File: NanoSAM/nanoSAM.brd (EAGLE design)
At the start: 89.6 x 94 mm, 119 parts, among them J1 POWER_JACK, U1 LTC3260EMSEPBF, U2 LMV324

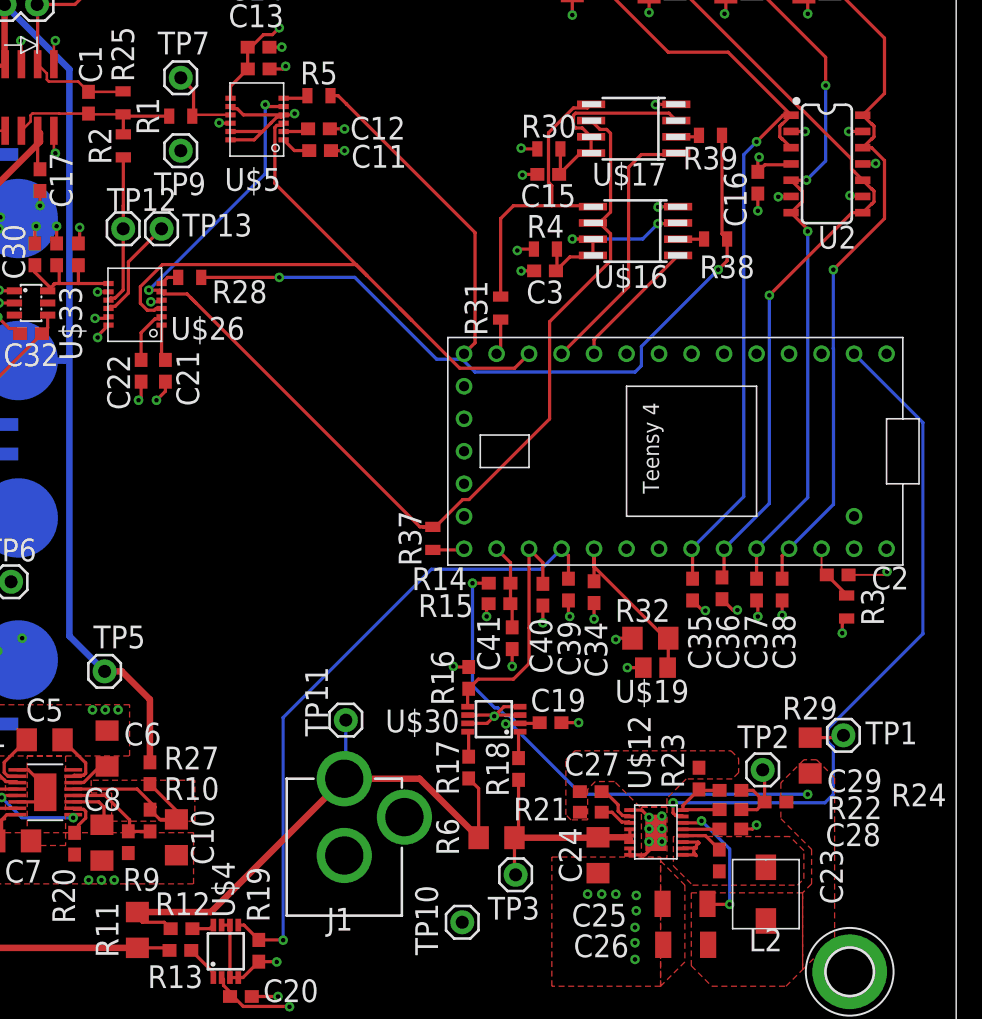
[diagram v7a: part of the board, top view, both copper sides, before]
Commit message: fixed footprint, broke other things
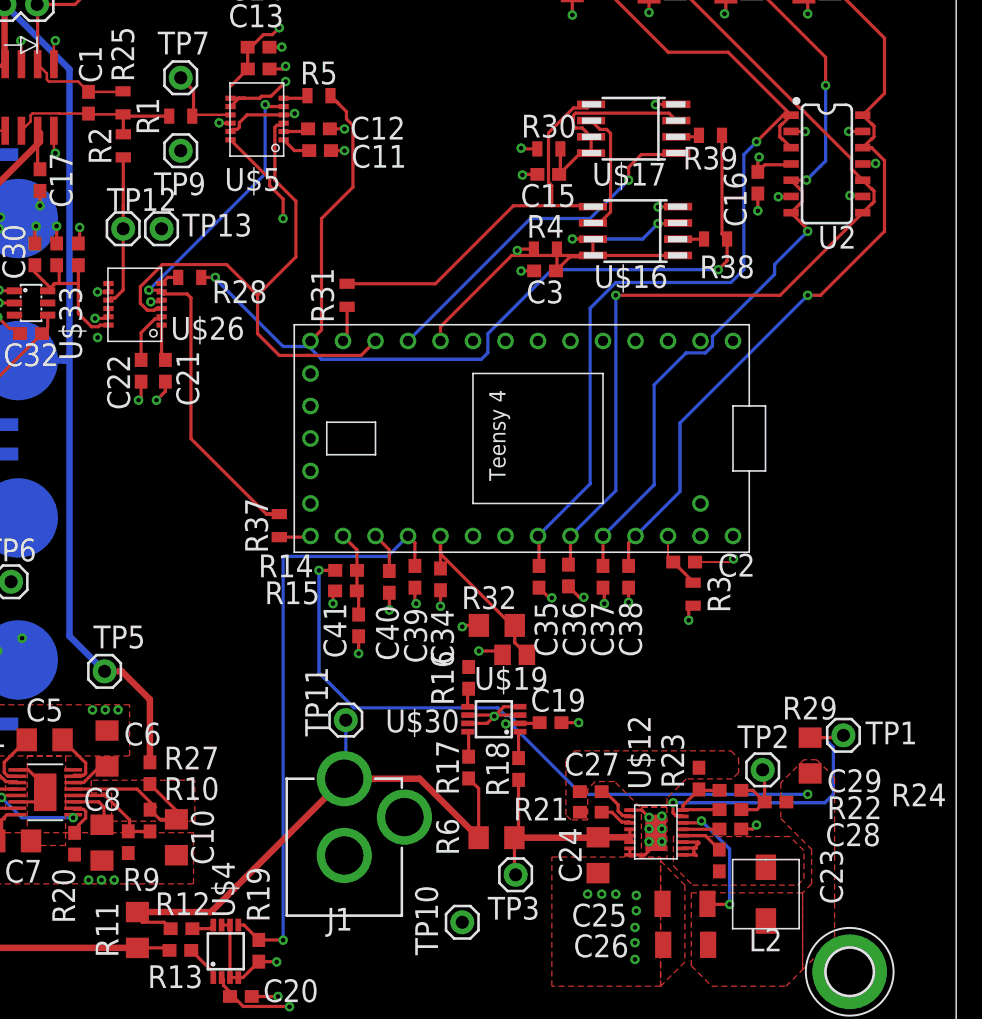
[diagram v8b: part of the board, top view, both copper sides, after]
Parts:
- moved C2 12.0 mm to (68.3, 36.1)
- moved C34 12.0 mm to (49.3, 34.8)
- moved C35 12.0 mm to (57.0, 35.0)
- moved C36 12.0 mm to (59.3, 35.1)
- moved C37 12.0 mm to (62.0, 35.0)
- moved C38 12.0 mm to (64.0, 35.0)
- moved C39 12.0 mm to (47.3, 35.0)
- moved C40 12.0 mm to (45.3, 34.6)
- moved C41 12.0 mm to (42.9, 31.2)
- moved R14 12.0 mm to (41.9, 35.5)
- moved R15 12.0 mm to (41.9, 33.9)
- moved R3 12.0 mm to (69.0, 33.6)
- moved R31 12.0 mm to (42.0, 57.0)
- moved R32 12.0 mm to (53.7, 31.2)
- moved R37 12.0 mm to (36.7, 39.0)
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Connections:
- net +3V3: now also U$5.P12; no longer U$5.P7
- net AGND: now also U$26.P7; no longer U$26.P12
- net DGND: now also U$5.P7; no longer U$5.P12
- net N$26: now also U$26.P12; no longer U$26.P7
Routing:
- net SPI_SCK: track 91.0 -> 54.3 mm
- net HK_3V3_PG: track 54.4 -> 18.8 mm
- net HK_3V3_C: track 19.1 -> 4.67 mm
- net N$28: track 50.0 -> 62.4 mm
- net FLASH_CS1: track 10.4 -> 22.0 mm
- net ADC_CS: track 54.9 -> 43.6 mm
- net HK_INST_THRM1: track 63.9 -> 74.9 mm
- net HK_INST_THRM0: track 67.9 -> 77.2 mm
- net SPI_MOSI: track 23.8 -> 31.8 mm
- net AGND: track 46.2 -> 38.3 mm
- net +3V3: track 35.7 -> 42.6 mm, vias 12 -> 13
- net FLASH_CS2: track 20.9 -> 27.6 mm, vias 0 -> 1
- net HK_INST_THRM2: track 59.2 -> 64.0 mm
- net SPI_MISO: track 84.7 -> 79.9 mm
- net HK_INST_THRM3: track 59.7 -> 64.3 mm
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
